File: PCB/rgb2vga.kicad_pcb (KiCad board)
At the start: 2 copper layers, 74.8 x 55.9 mm, 41 parts, among them J1 GPIO_0, J2 RGB_IN, J3 COCO3_RGB_IN, J4 C_VIDEO_IN, J5 GPIO_1, J6 VGA_OUT, SW1 SW_DIP_x08, U1 LM1881

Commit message: add DE0-Nano virtual component
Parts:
- added REF**: DE0-Nano, 000_LOCAL:DE0-Nano, F.Cu at (143.7, 103.8)
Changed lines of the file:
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@@
     (tracks 247)
     (zones 0)
-    (modules 41)
+    (modules 42)
     (nets 47)
   )
@@
     (add_net GND)
     (add_net "Net-(C1-Pad2)")
-    (add_net "Net-(J1-Pad10)")
     (add_net "Net-(J1-Pad13)")
-    (add_net "Net-(J1-Pad14)")
     (add_net "Net-(J1-Pad15)")
-    (add_net "Net-(J1-Pad16)")
     (add_net "Net-(J1-Pad17)")
-    (add_net "Net-(J1-Pad18)")
     (add_net "Net-(J1-Pad19)")
-    (add_net "Net-(J1-Pad20)")
     (add_net "Net-(J1-Pad21)")
-    (add_net "Net-(J1-Pad22)")
     (add_net "Net-(J1-Pad23)")
-    (add_net "Net-(J1-Pad24)")
     (add_net "Net-(J1-Pad25)")
-    (add_net "Net-(J1-Pad26)")
     (add_net "Net-(J1-Pad27)")
-    (add_net "Net-(J1-Pad28)")
-    (add_net "Net-(J1-Pad29)")
-    (add_net "Net-(J1-Pad33)")
-    (add_net "Net-(J1-Pad34)")
-    (add_net "Net-(J1-Pad35)")
-    (add_net "Net-(J1-Pad36)")
-    (add_net "Net-(J1-Pad5)")
-    (add_net "Net-(J1-Pad7)")
-    (add_net "Net-(J1-Pad9)")
-    (add_net "Net-(J2-Pad11)")
-    (add_net "Net-(J2-Pad12)")
-    (add_net "Net-(J2-Pad14)")
-    (add_net "Net-(J2-Pad15)")
-    (add_net "Net-(J3-Pad10)")
-    (add_net "Net-(J3-Pad6)")
-    (add_net "Net-(J3-Pad7)")
-    (add_net "Net-(J5-Pad1)")
-    (add_net "Net-(J5-Pad11)")
-    (add_net "Net-(J5-Pad13)")
-    (add_net "Net-(J5-Pad17)")
-    (add_net "Net-(J5-Pad19)")
-    (add_net "Net-(J5-Pad2)")
-    (add_net "Net-(J5-Pad21)")
-    (add_net "Net-(J5-Pad23)")
-    (add_net "Net-(J5-Pad25)")
-    (add_net "Net-(J5-Pad27)")
-    (add_net "Net-(J5-Pad29)")
-    (add_net "Net-(J5-Pad3)")
-    (add_net "Net-(J5-Pad31)")
-    (add_net "Net-(J5-Pad32)")
-    (add_net "Net-(J5-Pad33)")
-    (add_net "Net-(J5-Pad34)")
-    (add_net "Net-(J5-Pad35)")
-    (add_net "Net-(J5-Pad36)")
-    (add_net "Net-(J5-Pad37)")
-    (add_net "Net-(J5-Pad38)")
-    (add_net "Net-(J5-Pad39)")
-    (add_net "Net-(J5-Pad4)")
-    (add_net "Net-(J5-Pad40)")
-    (add_net "Net-(J5-Pad5)")
-    (add_net "Net-(J5-Pad6)")
-    (add_net "Net-(J5-Pad7)")
-    (add_net "Net-(J5-Pad9)")
-    (add_net "Net-(J6-Pad11)")
-    (add_net "Net-(J6-Pad12)")
     (add_net "Net-(J6-Pad13)")
     (add_net "Net-(J6-Pad14)")
-    (add_net "Net-(J6-Pad15)")
-    (add_net "Net-(J6-Pad4)")
     (add_net "Net-(JP2-Pad1)")
     (add_net "Net-(JP3-Pad1)")
     (add_net "Net-(R12-Pad2)")
     (add_net "Net-(R14-Pad2)")
-    (add_net "Net-(R24-Pad3)")
-    (add_net "Net-(U1-Pad5)")
-    (add_net "Net-(U1-Pad7)")
+  )
+  (module 000_LOCAL:DE0-Nano (layer Top)
+    (at 143.7 103.765 270)
+    (attr virtual)
+    (fp_text reference REF** (at 0 2 90) (layer F.SilkS) hide
+      (effects (font (size 4 4) (thickness 0.12)))
+    )
+    (fp_text value DE0-Nano (at 0 -2 90) (layer F.Fab)
+      (effects (font (size 1 1) (thickness 0.1)))
+    )
+    (fp_line (start -37.59 -24.51) (end 37.59 -24.51) (layer Dwgs.User) (width 0.1))
+    (fp_line (start -37.59 24.51) (end 37.59 24.51) (layer Dwgs.User) (width 0.1))
+    (fp_line (start -37.59 -24.51) (end -37.59 24.51) (layer Dwgs.User) (width 0.1))
+    (fp_line (start 37.59 -24.51) (end 37.59 24.51) (layer Dwgs.User) (width 0.1))
+    (fp_line (start 28.19 3.71) (end 37.59 3.71) (layer Dwgs.User) (width 0.1))
+    (fp_line (start 37.59 11.51) (end 28.19 11.51) (layer Dwgs.User) (width 0.1))
+    (fp_line (start 28.19 11.51) (end 28.19 3.71) (layer Dwgs.User) (width 0.1))
+    (model ${KIPRJMOD}/000_LOCAL.pretty/3dshapes/DE0-Nano.step
+      (offset (xyz 0 0 -14.5))
+      (scale (xyz 1 1 1))
+      (rotate (xyz 0 0 0))
+    )
   )
   (module 000_LOCAL:C025-025X050 (layer Top)
@@
       (effects (font (size 0.8 0.8) (thickness 0.1)) (justify bottom))
     )
-    (fp_arc (start -2.159 1.016) (end -2.413 1.016) (angle -90) (layer F.SilkS) (width 0.1524))
-    (fp_arc (start 2.159 1.016) (end 2.159 1.27) (angle -90) (layer F.SilkS) (width 0.1524))
-    (fp_arc (start -2.159 -1.016) (end -2.413 -1.016) (angle 90) (layer F.SilkS) (width 0.1524))
-    (fp_arc (start 2.159 -1.016) (end 2.159 -1.27) (angle 90) (layer F.SilkS) (width 0.1524))
     (fp_line (start -0.381 0) (end -0.762 0) (layer F.Fab) (width 0.1524))
     (fp_line (start -0.254 0) (end -0.381 0) (layer F.SilkS) (width 0.1524))
@@
     (fp_line (start 2.159 1.27) (end -2.159 1.27) (layer F.SilkS) (width 0.1524))
     (fp_line (start -2.159 -1.27) (end 2.159 -1.27) (layer F.SilkS) (width 0.1524))
+    (fp_arc (start -2.159 1.016) (end -2.413 1.016) (angle -90) (layer F.SilkS) (width 0.1524))
+    (fp_arc (start 2.159 1.016) (end 2.159 1.27) (angle -90) (layer F.SilkS) (width 0.1524))
+    (fp_arc (start -2.159 -1.016) (end -2.413 -1.016) (angle 90) (layer F.SilkS) (width 0.1524))
+    (fp_arc (start 2.159 -1.016) (end 2.159 -1.27) (angle 90) (layer F.SilkS) (width 0.1524))
     (pad 2 thru_hole circle (at 1.27 0) (size 1.3208 1.3208) (drill 0.8128) (layers *.Cu *.Mask)
       (net 46 "Net-(C1-Pad2)") (solder_mask_margin 0.1016))
@@
       (effects (font (size 0.8 0.8) (thickness 0.1)) (justify bottom))
     )
-    (fp_arc (start -2.159 1.016) (end -2.413 1.016) (angle -90) (layer F.SilkS) (width 0.1524))
-    (fp_arc (start 2.159 1.016) (end 2.159 1.27) (angle -90) (layer F.SilkS) (width 0.1524))
-    (fp_arc (start -2.159 -1.016) (end -2.413 -1.016) (angle 90) (layer F.SilkS) (width 0.1524))
-    (fp_arc (start 2.159 -1.016) (end 2.159 -1.27) (angle 90) (layer F.SilkS) (width 0.1524))
     (fp_line (start -0.381 0) (end -0.762 0) (layer F.Fab) (width 0.1524))
     (fp_line (start -0.254 0) (end -0.381 0) (layer F.SilkS) (width 0.1524))
@@
     (fp_line (start 2.159 1.27) (end -2.159 1.27) (layer F.SilkS) (width 0.1524))
     (fp_line (start -2.159 -1.27) (end 2.159 -1.27) (layer F.SilkS) (width 0.1524))
+    (fp_arc (start -2.159 1.016) (end -2.413 1.016) (angle -90) (layer F.SilkS) (width 0.1524))
+    (fp_arc (start 2.159 1.016) (end 2.159 1.27) (angle -90) (layer F.SilkS) (width 0.1524))
+    (fp_arc (start -2.159 -1.016) (end -2.413 -1.016) (angle 90) (layer F.SilkS) (width 0.1524))
+    (fp_arc (start 2.159 -1.016) (end 2.159 -1.27) (angle 90) (layer F.SilkS) (width 0.1524))
     (pad 2 thru_hole circle (at 1.27 0) (size 1.3208 1.3208) (drill 0.8128) (layers *.Cu *.Mask)
       (net 3 /RSET) (solder_mask_margin 0.1016))
@@
   (segment (start 134.62 86.995) (end 128.27 86.995) (width 0.3048) (layer Top) (net 2))
   (segment (start 144.78 76.835) (end 134.62 86.995) (width 0.3048) (layer Top) (net 2))
-  (segment (start 157.988 104.902) (end 157.988 103.57) (width 0.3048) (layer Top) (net 46))
-  (segment (start 157.353 105.537) (end 157.988 104.902) (width 0.3048) (layer Top) (net 46))
-  (segment (start 154.432 105.537) (end 157.353 105.537) (width 0.3048) (layer Top) (net 46))
-  (segment (start 153.035 104.14) (end 154.432 105.537) (width 0.3048) (layer Top) (net 46))
   (segment (start 153.035 107.95) (end 149.86 111.125) (width 0.3048) (layer Top) (net 3))
   (segment (start 155.067 109.982) (end 153.035 107.95) (width 0.3048) (layer Top) (net 3))
@@
   (segment (start 175.895 99.389) (end 175.895 86.2965) (width 0.3048) (layer Bottom) (net 45))
   (segment (start 174.065 101.219) (end 175.895 99.389) (width 0.3048) (layer Bottom) (net 45))
+  (segment (start 157.988 104.902) (end 157.988 103.57) (width 0.3048) (layer Top) (net 46))
+  (segment (start 157.353 105.537) (end 157.988 104.902) (width 0.3048) (layer Top) (net 46))
+  (segment (start 154.432 105.537) (end 157.353 105.537) (width 0.3048) (layer Top) (net 46))
+  (segment (start 153.035 104.14) (end 154.432 105.537) (width 0.3048) (layer Top) (net 46))
   (zone (net 1) (net_name GND) (layer Top) (hatch edge 0.508)
     (priority 6)

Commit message: low profile version
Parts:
- removed JP1, JP2, JP3: Jumper_2_Open, 000_LOCAL:JP
- removed the REF** at (143.7, 103.8)
- added REF**: DE0-Nano_no_cover, 000_LOCAL:DE0-Nano_no_cover, F.Cu at (143.6, 103.6)
- J2, J3, J4, J6: moved to B.Cu
- R24: footprint 000_LOCAL:PT-10 -> 000_LOCAL:PT10Lx-hole; moved to B.Cu
- SW1: value SW_DIP_x08 -> SW_DIP_x12; footprint 000_LOCAL:SW_DIP_SPSTx08_Slide_9.78x22.5mm_W7.62mm_P2.54mm -> 000_LOCAL:SW_DIP_SPSTx12_Slide_6.7x32.04mm_W8.61mm_P2.54mm_LowProfile
- moved J4 71.0 mm to (171.4, 82.5), turned to 90 degrees
- moved J2 11.7 mm to (113.0, 111.1), turned to 90 degrees
- moved R27 11.4 mm to (117.7, 110.5)
- moved J6 10.9 mm to (173.4, 111.8), turned to 270 degrees
- moved R28 10.8 mm to (117.7, 121.9)
- moved SW1 8.52 mm to (130.8, 99.7)
- moved J3 7.39 mm to (114.9, 80.0), turned to 180 degrees
- turned R24 to 180 degrees
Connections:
- R24 pad 1: /DIFF_N -> (no net)
- R24 pad 3: (no net) -> /DIFF_N
- SW1 pad 1: Net-(J1-Pad27) -> (no net)
- SW1 pad 10: GND -> Net-(J1-Pad13)
- SW1 pad 11: GND -> /_HSYNC
- SW1 pad 12: GND -> /_VSYNC
- SW1 pad 13: GND -> Net-(SW1-Pad13)
- SW1 pad 14: GND -> Net-(SW1-Pad14)
- SW1 pad 2: Net-(J1-Pad25) -> /DIFFG
- SW1 pad 3: Net-(J1-Pad23) -> Net-(J1-Pad27)
- SW1 pad 4: Net-(J1-Pad21) -> Net-(J1-Pad25)
- SW1 pad 5: Net-(J1-Pad19) -> Net-(J1-Pad23)
- SW1 pad 6: Net-(J1-Pad17) -> Net-(J1-Pad21)
- SW1 pad 7: Net-(J1-Pad15) -> Net-(J1-Pad19)
- SW1 pad 8: Net-(J1-Pad13) -> Net-(J1-Pad17)
- SW1 pad 9: GND -> Net-(J1-Pad15)
- U1 pad 1: Net-(JP2-Pad1) -> Net-(SW1-Pad14)
- U1 pad 3: Net-(JP3-Pad1) -> Net-(SW1-Pad13)
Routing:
- net Net-(SW1-Pad14): track 0.00 -> 34.3 mm
- net /DIFFG: track 83.9 -> 115.2 mm, vias 0 -> 2
- net Net-(SW1-Pad13): track 0.00 -> 30.8 mm
- net Net-(JP2-Pad1): track 29.2 -> 0.00 mm
- net /_HSYNC: track 61.1 -> 36.5 mm
- net Net-(JP3-Pad1): track 23.2 -> 0.00 mm
- net /_VSYNC: track 49.4 -> 27.4 mm
- net /CSYNC: track 84.5 -> 68.6 mm, vias 0 -> 1
- net /GREEN: track 24.3 -> 39.9 mm
- net /RED: track 15.9 -> 28.3 mm
- net Net-(J6-Pad13): track 34.9 -> 47.2 mm
- net /VSYNC: track 49.3 -> 38.3 mm, vias 0 -> 1
- net /_BRIGHT: track 14.5 -> 4.45 mm
- net /BLUE: track 34.6 -> 44.0 mm
- net /HSYNC: track 60.7 -> 53.1 mm, vias 1 -> 0
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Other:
- board size 74.8 x 55.9 mm -> 70.5 x 55.9 mm
- board text added: "CSYNC"
- board text added: "C_VIDEO"
- board text added: "github.com/bkw777/rgb2vga - v004"
- board text removed: "AUDIO"
- board text removed: "B"
- board text removed: "G"
- board text removed: "GND"
- board text removed: "H"
- board text removed: "JP1: C_VIDEO"
- board text removed: "JP2+JP3: CSYNC"
- board text removed: "PB3"
- board text removed: "R"
- board text removed: "V"
- board text removed: "github.com/bkw777/rgb2vga - v003"

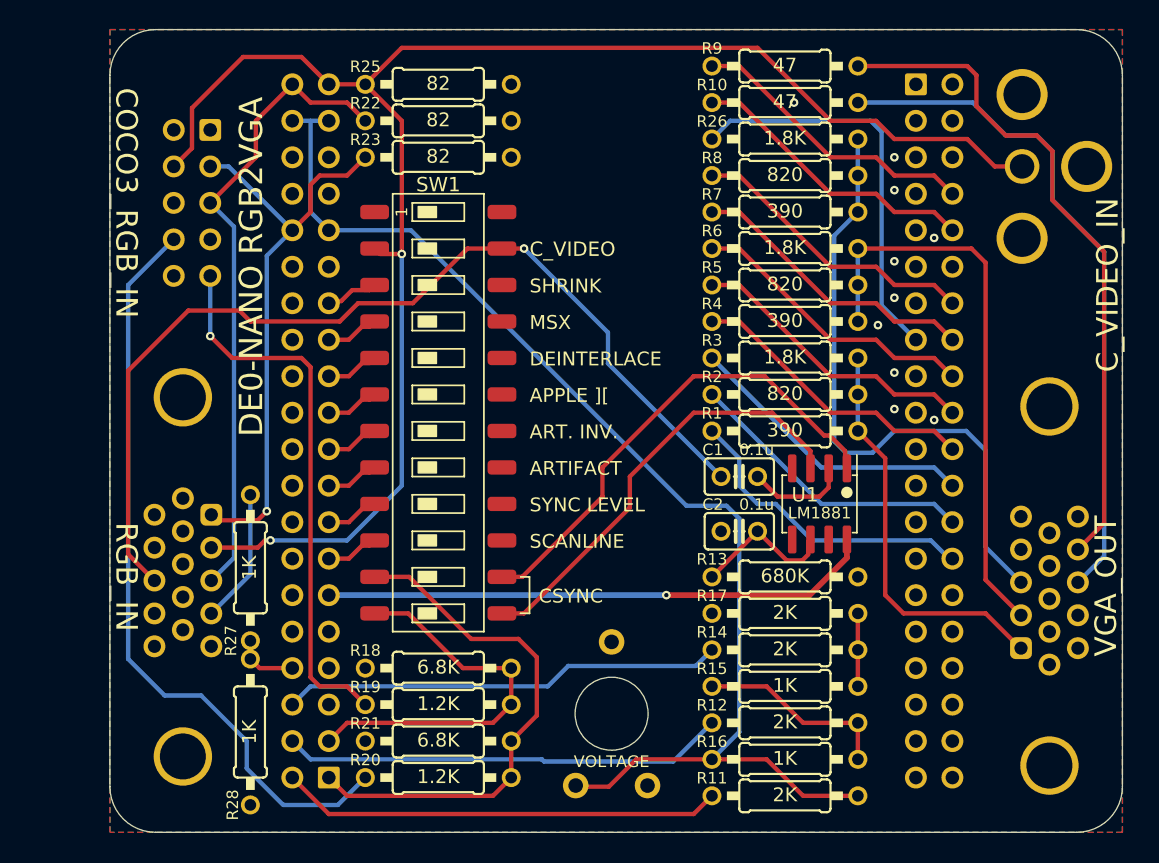
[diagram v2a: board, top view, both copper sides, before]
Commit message: renders, small routing touchup
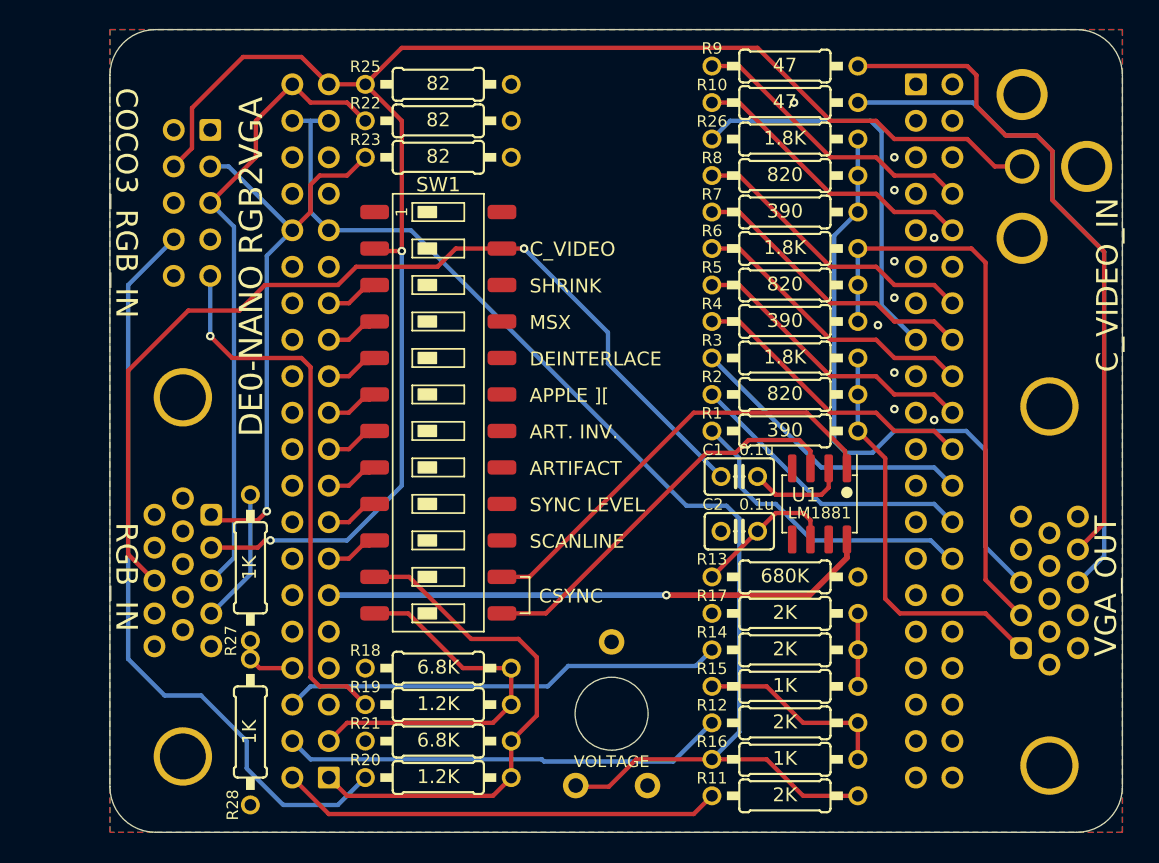
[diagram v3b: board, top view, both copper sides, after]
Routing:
- net Net-(SW1-Pad14): track 34.3 -> 31.0 mm
- net Net-(SW1-Pad13): track 30.8 -> 28.0 mm
- net /CSYNC: track 68.6 -> 68.0 mm

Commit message: silkscreen
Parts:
- moved C1 7.65 mm to (159.4, 104.8)
- moved C2 7.65 mm to (159.4, 107.3)
- moved U1 5.59 mm to (151.8, 106.0), turned to 0 degrees
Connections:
- C2 pad 1: GND -> /RSET
- C2 pad 2: /RSET -> GND
- R13 pad 1: /RSET -> GND
- R13 pad 2: GND -> /RSET
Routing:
- net Net-(SW1-Pad14): track 31.0 -> 16.9 mm
- net Net-(SW1-Pad13): track 28.0 -> 16.9 mm
- net /CSYNC: track 68.0 -> 74.6 mm
- net Net-(C1-Pad2): track 7.02 -> 13.2 mm
- net /DIFFR: track 40.4 -> 38.0 mm
- net +5V: track 38.4 -> 36.1 mm
- net /RSET: track 10.2 -> 8.74 mm
- net /DIFF_N: track 86.7 -> 85.2 mm
- net /R2: track 21.5 -> 20.4 mm
- net GND: vias 10 -> 14
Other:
- board text added: "RGB"
- board text added: "TO"
- board text added: "VGA"
- board text removed: "DE0-NANO RGB2VGA"

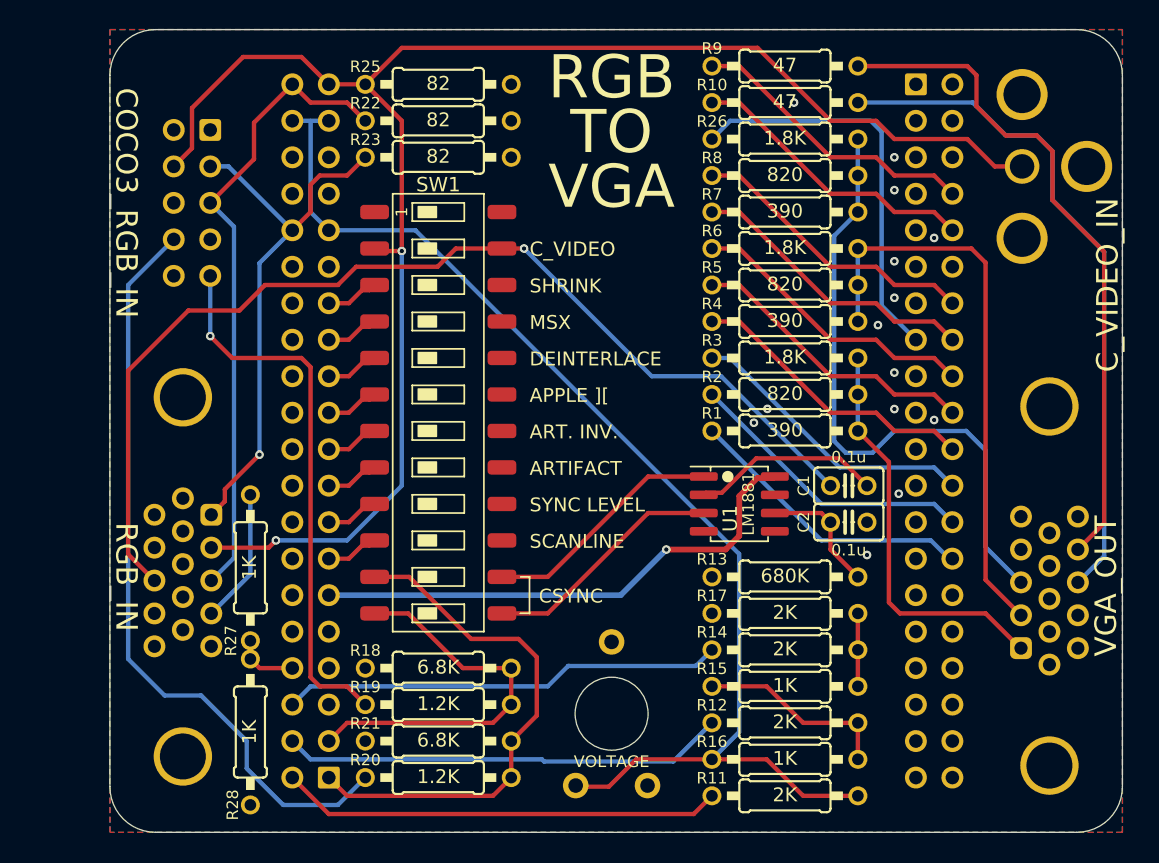
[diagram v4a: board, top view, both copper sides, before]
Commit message: net names, clearance for idc plugs around gpio headers
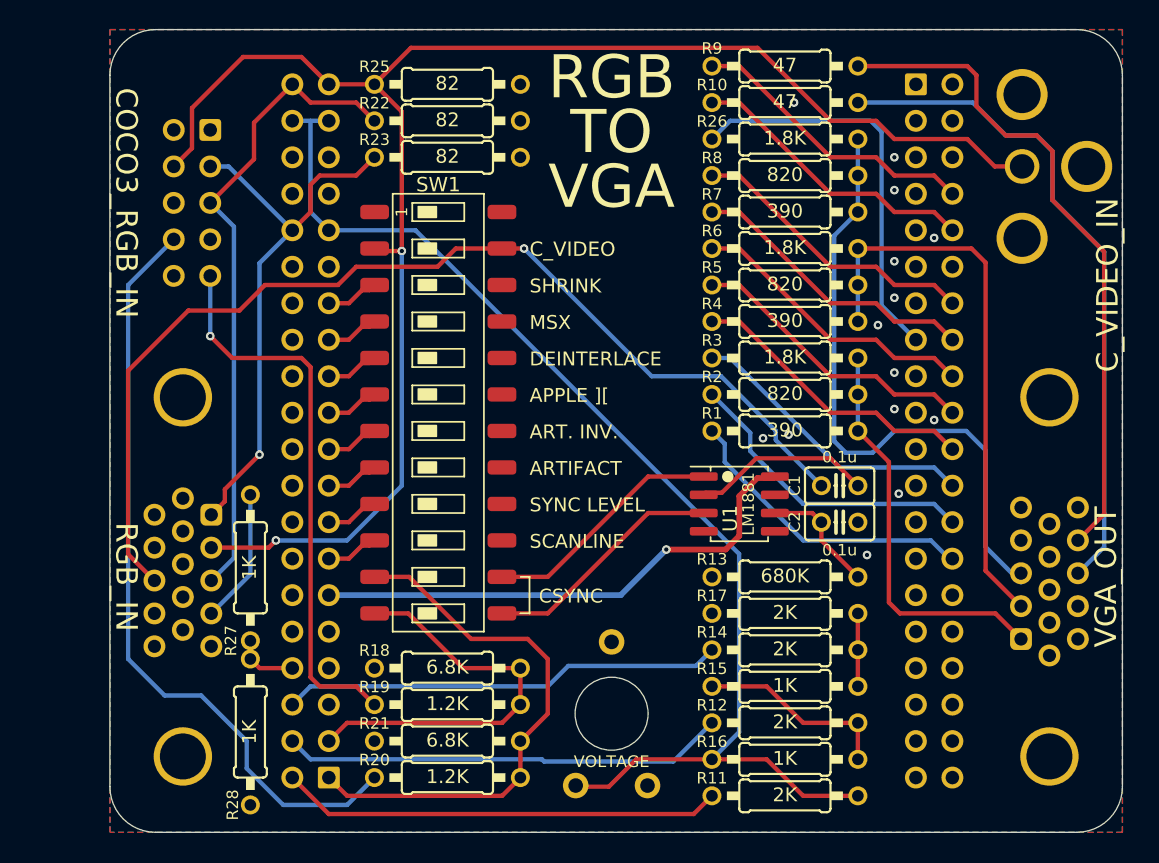
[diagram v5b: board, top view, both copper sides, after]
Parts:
- moved J6 0.64 mm to (173.4, 111.1)
- moved C1 0.63 mm to (158.8, 104.8)
- moved C2 0.63 mm to (158.8, 107.3)
- moved R18 0.63 mm to (131.4, 117.5)
- moved R19 0.63 mm to (131.4, 120.0)
- moved R20 0.63 mm to (131.4, 125.1)
- moved R21 0.63 mm to (131.4, 122.6)
- moved R22 0.63 mm to (131.4, 79.4)
- moved R23 0.63 mm to (131.4, 81.9)
- moved R25 0.63 mm to (131.4, 76.8)
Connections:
- net /BLUE renamed /VGA_B
- net /BRIGHT renamed /RGB_BR
- net /CSYNC renamed /RGB_CS
- net /DIFFB renamed /RGB_B
- net /DIFFG renamed /RGB_G
- net /DIFFR renamed /RGB_R
- net /GREEN renamed /VGA_G
- net /HSYNC renamed /RGB_H
- net /RED renamed /VGA_R
- net /VSYNC renamed /RGB_V
- net Net-(J1-Pad13) renamed /SW_SCANLINE
- net Net-(J1-Pad15) renamed /SW_SYNC_LVL
- net Net-(J1-Pad17) renamed /SW_ARTIFACT
- net Net-(J1-Pad19) renamed /SW_ARTIF_INV
- net Net-(J1-Pad21) renamed /SW_APPLE_][
- net Net-(J1-Pad23) renamed /SW_DEINT
- net Net-(J1-Pad25) renamed /SW_MSX
- net Net-(J1-Pad27) renamed /SW_SHRINK
- net Net-(J6-Pad13) renamed /VGA_H
- net Net-(J6-Pad14) renamed /VGA_V
- net Net-(SW1-Pad13) renamed /SW_C_VS
- net Net-(SW1-Pad14) renamed /SW_C_HS
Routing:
- net /_HSYNC: track 36.5 -> 37.9 mm
- net /_VSYNC: track 27.4 -> 28.7 mm
- net /R2: track 20.4 -> 21.2 mm
- net /R1: track 20.4 -> 21.2 mm
- net /VGA_H: track 47.2 -> 46.6 mm
- net /VGA_G: track 39.9 -> 39.3 mm
- net /RGB_V: track 38.3 -> 38.9 mm
- net /VGA_V: track 47.2 -> 46.6 mm
- net /RGB_R: track 38.0 -> 38.6 mm
- net /RGB_H: track 53.1 -> 53.8 mm
- net /RGB_B: track 44.4 -> 45.0 mm
- net Net-(C1-Pad2): track 13.2 -> 12.6 mm
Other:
- board text added: "github.com/bkw777/rgb2vga - v004.5"
- board text removed: "github.com/bkw777/rgb2vga - v004"
